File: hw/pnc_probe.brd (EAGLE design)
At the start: 35 x 40 mm, 14 parts, among them U1 TPS6024X_VSSOP8, U2 DUAL_NAND_SSOP8, U3 MF-DSC-SOT233-BSS138, X1 0446200002, X2 0446200002

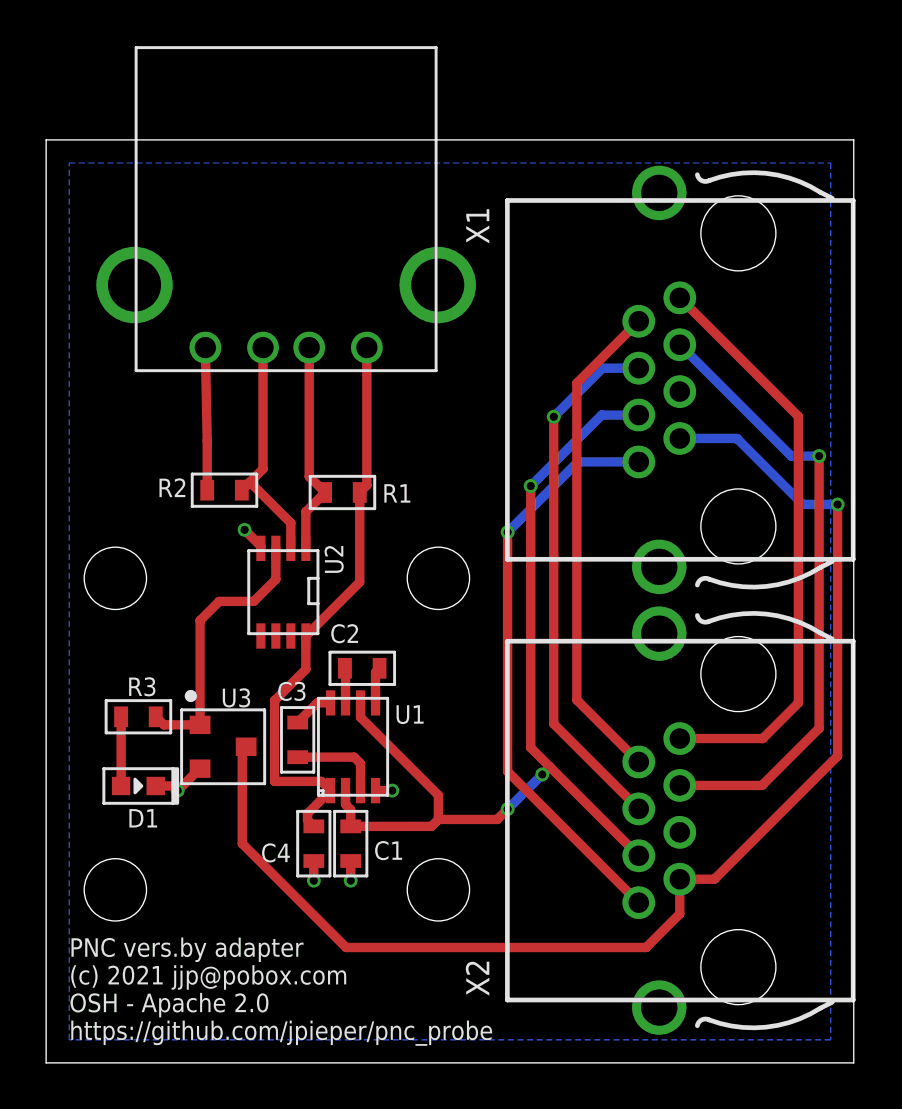
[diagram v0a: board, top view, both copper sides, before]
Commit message: Fix r1 errata
* The footprint for the TPS6024 was wrong.  I wasn't able to find a
  sample one, so used a generic VSSOP originally, but that didn't
  match the TI part.  I instead used rough dimensions from a KiCAD
  model and double checked against the datasheet.
* Yikes, I had left some airwires!
* Added test points for gnd, power, and the final probe signal.
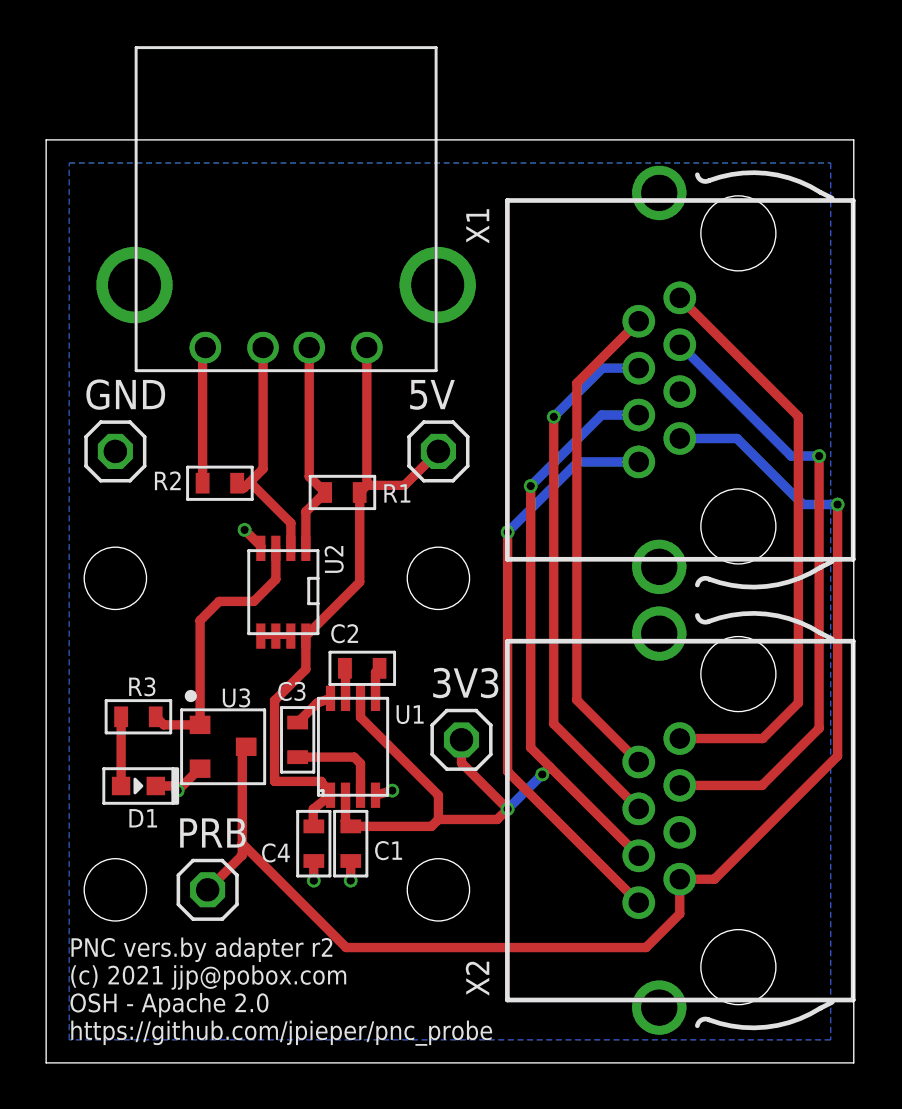
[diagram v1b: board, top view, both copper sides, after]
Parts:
- added 3V3, 5V, GND, PRB: (no value), pinhead:1X01
- moved R2 0.36 mm to (7.53, 25.1)
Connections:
- net GND: now also GND.1
- net PROBE: now also PRB.1
- net VCC_3V: now also 3V3.1
- net VCC_5V: now also 5V.1
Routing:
- net VCC_3V: track 41.7 -> 45.5 mm
- net VCC_5V: track 25.1 -> 28.6 mm
- net PROBE: track 55.2 -> 57.8 mm
- net N$1: track 0.00 -> 1.30 mm
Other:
- board text added: "PNC vers.by adapter r2 (c) 2021 jjp@pobox.com OSH - Apache 2.0 https://github.com/jpieper/pnc_probe"
- board text removed: "PNC vers.by adapter (c) 2021 jjp@pobox.com OSH - Apache 2.0 https://github.com/jpieper/pnc_probe"
